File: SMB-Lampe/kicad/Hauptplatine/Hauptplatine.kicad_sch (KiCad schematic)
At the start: 1 part, among them U1 MOUDLE-SEEEDUINO-XIAO-ESP32C3

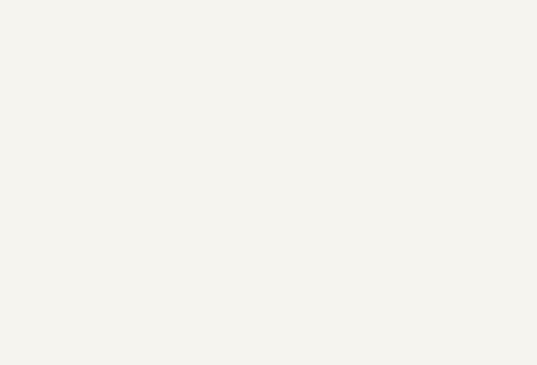
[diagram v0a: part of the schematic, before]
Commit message: Vorderes Hinterbein fertig
Alle Platinen sind fertig beschaltet
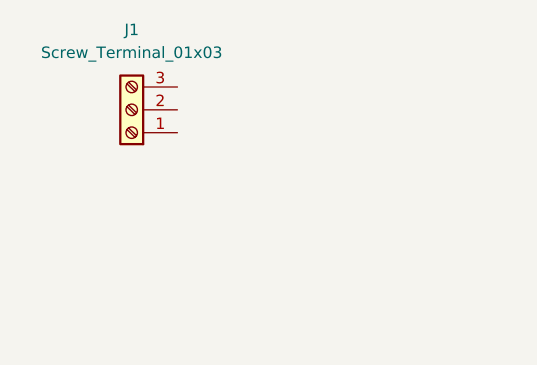
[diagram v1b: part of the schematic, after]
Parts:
- added J1: Screw_Terminal_01x03, w_conn_mkds:mkds_1,5-3, symbol Connector:Screw_Terminal_01x03
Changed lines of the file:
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@@
+	)
+	(symbol
+		(lib_id "Connector:Screw_Terminal_01x03")
+		(at 45.72 27.94 180)
+		(unit 1)
+		(exclude_from_sim no)
+		(in_bom yes)
+		(on_board yes)
+		(dnp no)
+		(fields_autoplaced yes)
+		(property "Reference" "J1"
+			(at 45.72 19.05 0)
+			(effects
+				(font
+					(size 1.27 1.27)
+				)
+			)
+		)
+		(property "Value" "Screw_Terminal_01x03"
+			(at 45.72 21.59 0)
+			(effects
+				(font
+					(size 1.27 1.27)
+				)
+			)
+		)
+		(property "Footprint" "w_conn_mkds:mkds_1,5-3"
+			(at 45.72 27.94 0)
+			(effects
+				(font
+					(size 1.27 1.27)
+				)
+				(hide yes)
+			)
+		)
+		(property "Datasheet" "~"
+			(at 45.72 27.94 0)
+			(effects
+				(font
+					(size 1.27 1.27)
+				)
+				(hide yes)
+			)
+		)
+		(property "Description" "Generic screw terminal, single row, 01x03, script generated (kicad-library-utils/schlib/autogen/connector/)"
+			(at 45.72 27.94 0)
+			(effects
+				(font
+					(size 1.27 1.27)
+				)
+				(hide yes)
+			)
+		)
+		(pin "1"
+		)
+		(pin "3"
+		)
+		(pin "2"
+		)
+		(instances
+			(project "Hauptplatine"
+				(path "/47d43428-8b74-42e4-922b-c564d80da2e6"
+					(reference "J1")
+					(unit 1)
+				)
+			)
+			(project ""
+				(path "/4831ca1b-de6c-4f01-b2f4-c7955e9e85c5/cefd35d6-050b-4482-ab35-5902e09a69d9"
+					(reference "J12")
+					(unit 1)
+				)
+			)
+		)
 	)
 	(symbol
@@
 		)
 		(instances
+			(project "Hauptplatine"
+				(path "/47d43428-8b74-42e4-922b-c564d80da2e6"
+					(reference "U1")
+					(unit 1)
+				)
+			)
 			(project "SMB-Lampe"
 				(path "/4831ca1b-de6c-4f01-b2f4-c7955e9e85c5/cefd35d6-050b-4482-ab35-5902e09a69d9"
@@
 		)
 	)
+	(sheet_instances
+		(path "/"
+			(page "1")
+		)
+	)
+	(embedded_fonts no)
 )

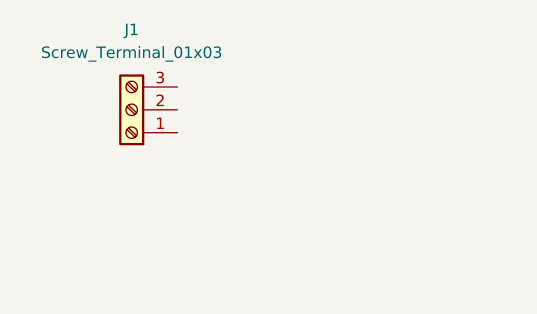
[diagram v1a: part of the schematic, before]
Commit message: Hinterbeine Geändert teilweiße Körper
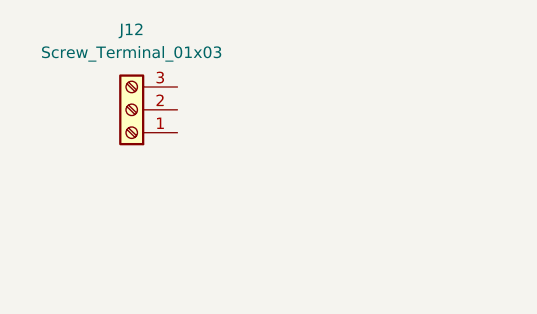
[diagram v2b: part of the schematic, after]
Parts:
- renumbered J1 to J12
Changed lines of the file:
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@@
 		(dnp no)
 		(fields_autoplaced yes)
-		(property "Reference" "J1"
+		(property "Reference" "J12"
 			(at 45.72 19.05 0)
 			(effects

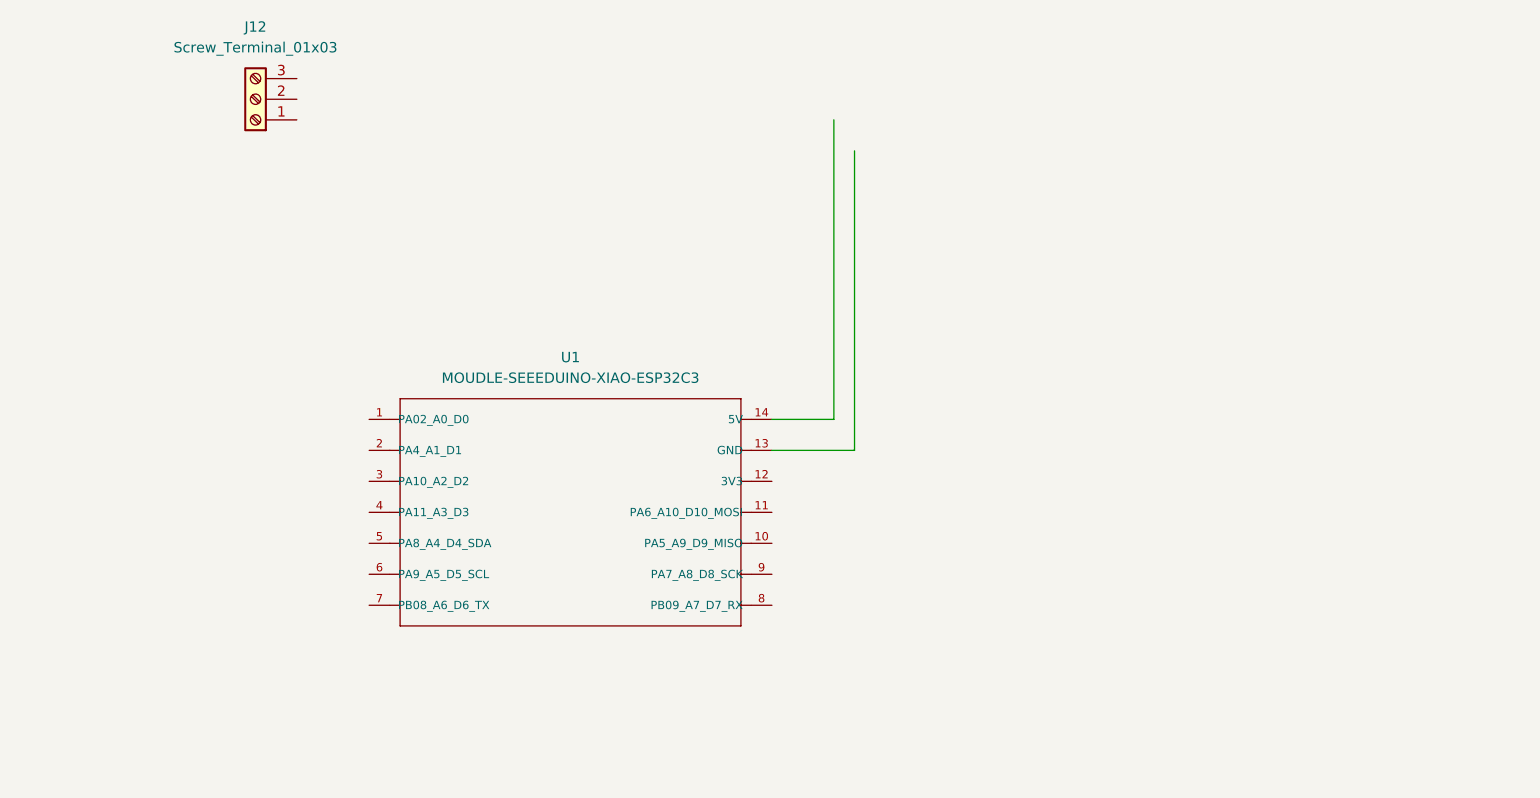
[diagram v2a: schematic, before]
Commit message: Hauptplatine fertig
Hauptplatine mit ESP Levelshifter und Screwsockets
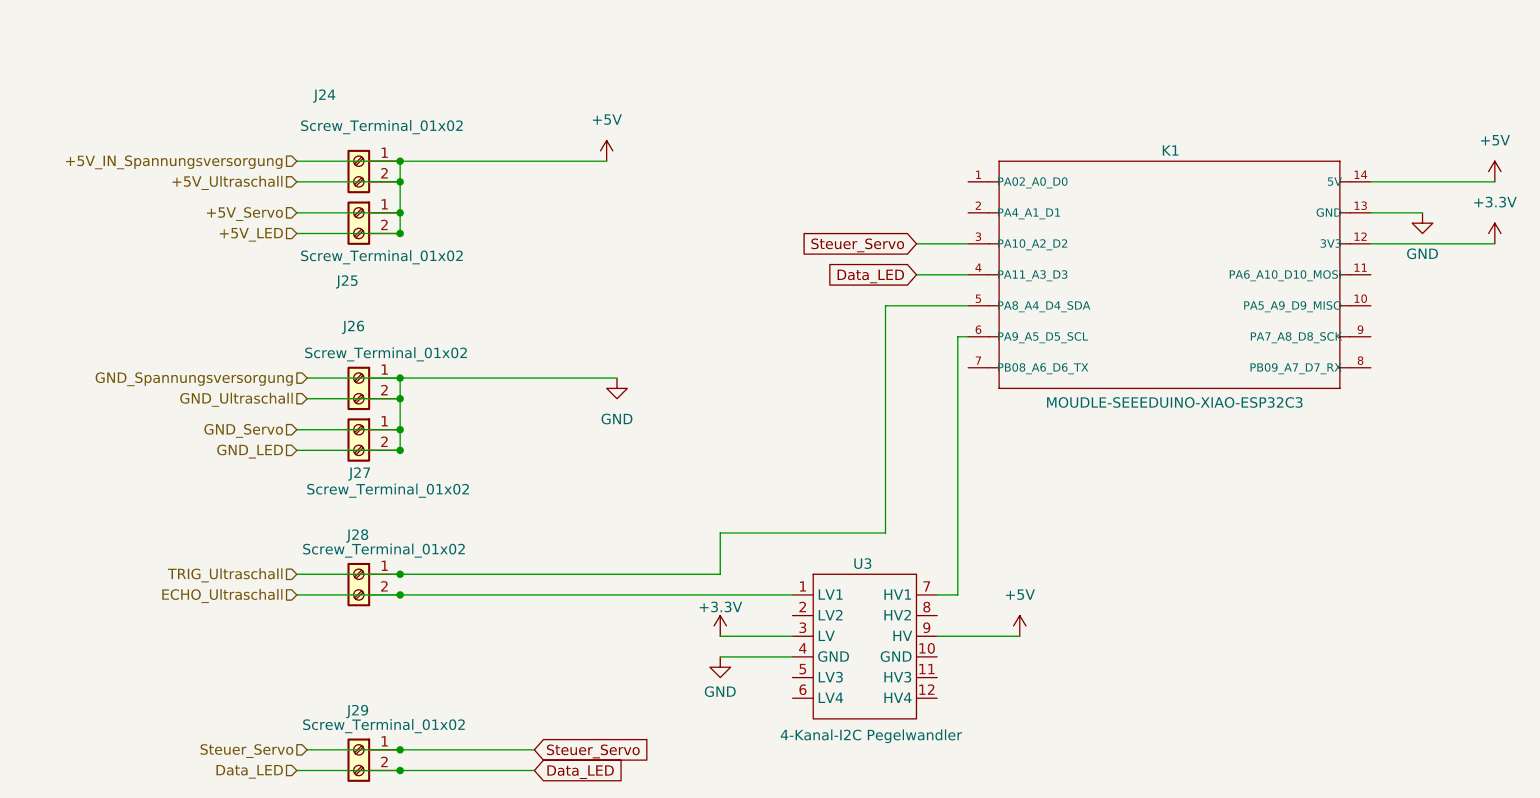
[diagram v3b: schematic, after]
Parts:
- removed J12: Screw_Terminal_01x03, w_conn_mkds:mkds_1,5-3, symbol Connector:Screw_Terminal_01x03
- added J24, J25, J26, J27, J28, J29: Screw_Terminal_01x02, Eigenen_Library:Screw Terminal, symbol Connector:Screw_Terminal_01x02
- added U3: 4-Kanal-I2C Pegelwandler, Eigenen_Library:I2C Levelshifter, symbol Eigene _Library:Levelshifter
- K1: renamed from U1; footprint xiao ESP32C3_PCB:MOUDLE14P-SMD-2.54-21X17.8MM -> Eigenen_Library:ESP32 C3
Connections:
- net +3.3V: now reaches K1.12 (3V3)
- net +3.3V: now also U3.3 (LV)
- net GND: now reaches K1.13 (GND)
- net GND: now also J26.1 (Pin_1), J26.2 (Pin_2), J27.1 (Pin_1), J27.2 (Pin_2), U3.4 (GND)
- net +5V: now reaches K1.14 (5V)
- net +5V: now also J24.1 (Pin_1), J24.2 (Pin_2), J25.1 (Pin_1), J25.2 (Pin_2), U3.9 (HV)
- net Steuer_Servo: now reaches K1.3 (PA10_A2_D2)
- net Steuer_Servo: now also J29.1 (Pin_1)
- net Data_LED: now reaches K1.4 (PA11_A3_D3)
- net Data_LED: now also J29.2 (Pin_2)
- net TRIG_Ultraschall: now reaches K1.5 (PA8_A4_D4_SDA)
- net TRIG_Ultraschall: now also J28.1 (Pin_1)
- net at K1.6 (PA9_A5_D5_SCL): now also U3.7 (HV1)
- new net ECHO_Ultraschall: J28.2 (Pin_2), U3.1 (LV1)
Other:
- moved on the sheet: K1

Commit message: Nachträgliche Änderungen für die Fertigung und Präsentation
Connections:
- net GND: now also U3.10 (GND); no longer U3.4 (GND)
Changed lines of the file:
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@@
+	(wire
+		(pts
+			(xy 129.54 96.52) (xy 139.7 96.52)
+		)
+		(stroke
+			(width 0)
+			(type default)
+		)
+	)
 	(wire
 		(pts
@@
 		(pts
 			(xy 50.8 38.1) (xy 63.5 38.1)
-		)
-		(stroke
-			(width 0)
-			(type default)
-		)
-	)
-	(wire
-		(pts
-			(xy 111.76 96.52) (xy 102.87 96.52)
 		)
 		(stroke
@@
 	(symbol
 		(lib_id "power:GND")
-		(at 102.87 96.52 0)
+		(at 139.7 96.52 0)
 		(unit 1)
 		(exclude_from_sim no)
@@
 		(dnp no)
 		(property "Reference" "#PWR035"
-			(at 102.87 102.87 0)
+			(at 139.7 102.87 0)
 			(effects
 				(font
@@
 		)
 		(property "Value" "GND"
-			(at 102.87 100.838 0)
+			(at 139.7 100.838 0)
 			(effects
 				(font
@@
 		)
 		(property "Footprint" ""
-			(at 102.87 96.52 0)
+			(at 139.7 96.52 0)
 			(effects
 				(font
@@
 		)
 		(property "Datasheet" ""
-			(at 102.87 96.52 0)
+			(at 139.7 96.52 0)
 			(effects
 				(font
@@
 		)
 		(property "Description" "Power symbol creates a global label with name \"GND\" , ground"
-			(at 102.87 96.52 0)
-			(effects
-				(font
+			(at 139.7 96.52 0)
+			(effects
+				(font

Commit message: vor Schaltplananpassung
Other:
- company: (none) -> IFM / Lukas Gulde
- title: (none) -> Projektaarbeit SMB-Lampe
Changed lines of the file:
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@@
 	(generator_version "9.0")
 	(paper "A4")
+	(title_block
+		(title "Projektaarbeit SMB-Lampe")
+		(date "2026-03-31")
+		(company "IFM / Lukas Gulde")
+		(comment 1 "Hauptplatine")
+	)
 	(junction
 		(at 63.5 86.36)
@@
 	(wire
 		(pts
-			(xy 63.5 86.36) (xy 102.87 86.36)
-		)
-		(stroke
-			(width 0)
-			(type default)
-		)
-	)
-	(wire
-		(pts
 			(xy 129.54 96.52) (xy 139.7 96.52)
 		)
@@
 	(wire
 		(pts
+			(xy 102.87 86.36) (xy 63.5 86.36)
+		)
+		(stroke
+			(width 0)
+			(type default)
+		)
+	)
+	(wire
+		(pts
 			(xy 50.8 35.56) (xy 63.5 35.56)
 		)
@@
 	(wire
 		(pts
-			(xy 123.19 81.28) (xy 102.87 81.28)
+			(xy 128.27 78.74) (xy 102.87 78.74)
 		)
 		(stroke
@@
 	(wire
 		(pts
-			(xy 123.19 53.34) (xy 133.35 53.34)
+			(xy 128.27 53.34) (xy 133.35 53.34)
 		)
 		(stroke
@@
 	(wire
 		(pts
-			(xy 123.19 81.28) (xy 123.19 53.34)
+			(xy 128.27 78.74) (xy 128.27 53.34)
 		)
 		(stroke
@@
 	(wire
 		(pts
-			(xy 102.87 81.28) (xy 102.87 86.36)
-		)
-		(stroke
+			(xy 102.87 78.74) (xy 102.87 86.36)
+		)
+		(stroke
